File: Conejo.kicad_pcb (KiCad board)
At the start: 4 copper layers, 130.3 x 112.5 mm, 104 parts, among them J1 BATT, J2 HRO_TYPE-C-31-M-12, J3 JTAG_TC2030, J4 RGB, Q1 2N7002, Q2 2N7002, Q3 AO3407, SW1 POWER, SW10 MX Hotswap, SW11 MX Hotswap, SW12 MX Hotswap, SW13 MX Hotswap, SW14 MX Hotswap, SW15 MX Hotswap, SW16 MX Hotswap, SW17 MX Hotswap, SW18 MX Hotswap, SW19 MX Hotswap, SW2 MX Hotswap, SW20 MX Hotswap, SW21 MX Hotswap, SW22 MX Hotswap, SW23 MX Hotswap, SW24 MX Hotswap, SW25 MX Hotswap, SW26 MX Hotswap, SW27 MX Hotswap, SW28 MX Hotswap, SW29 RESET, SW3 MX Hotswap, SW4 MX Hotswap, SW5 MX Hotswap, SW6 MX Hotswap, SW7 MX Hotswap, SW8 MX Hotswap, SW9 MX Hotswap, U1 BQ24075RGT, U2 MAX17048, U3 SRV05-4, U4 MS88SF3

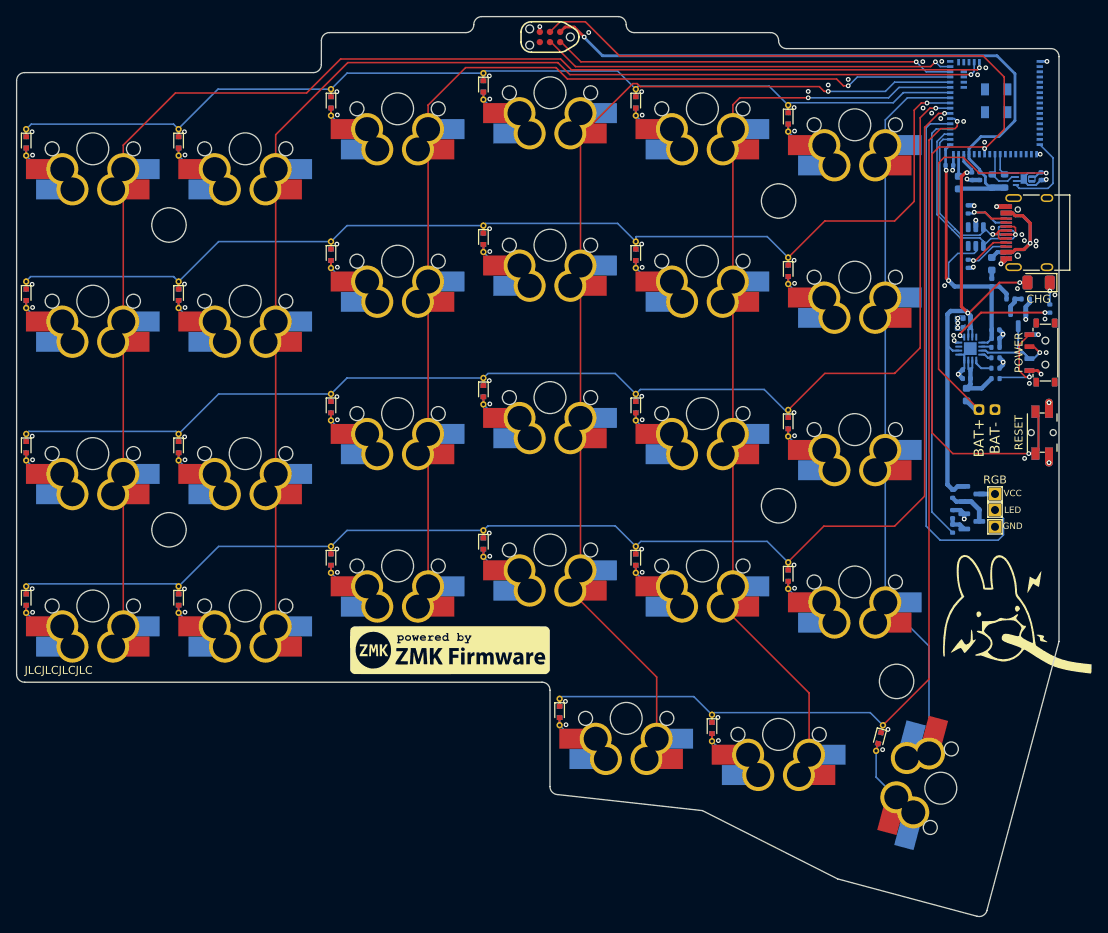
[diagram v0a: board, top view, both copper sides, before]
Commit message: feat(pcb): Version 0.4
- Prepare to move from JLC7628 stackup to JLC3313 stackup (Lowers dielectric constant from 4.6 to 4.05)
- Increase mounting hole diameter back to 5.4mm
- 6mil signals, 10mil power, 13 mil vias
  - 3W spacing wherever possible
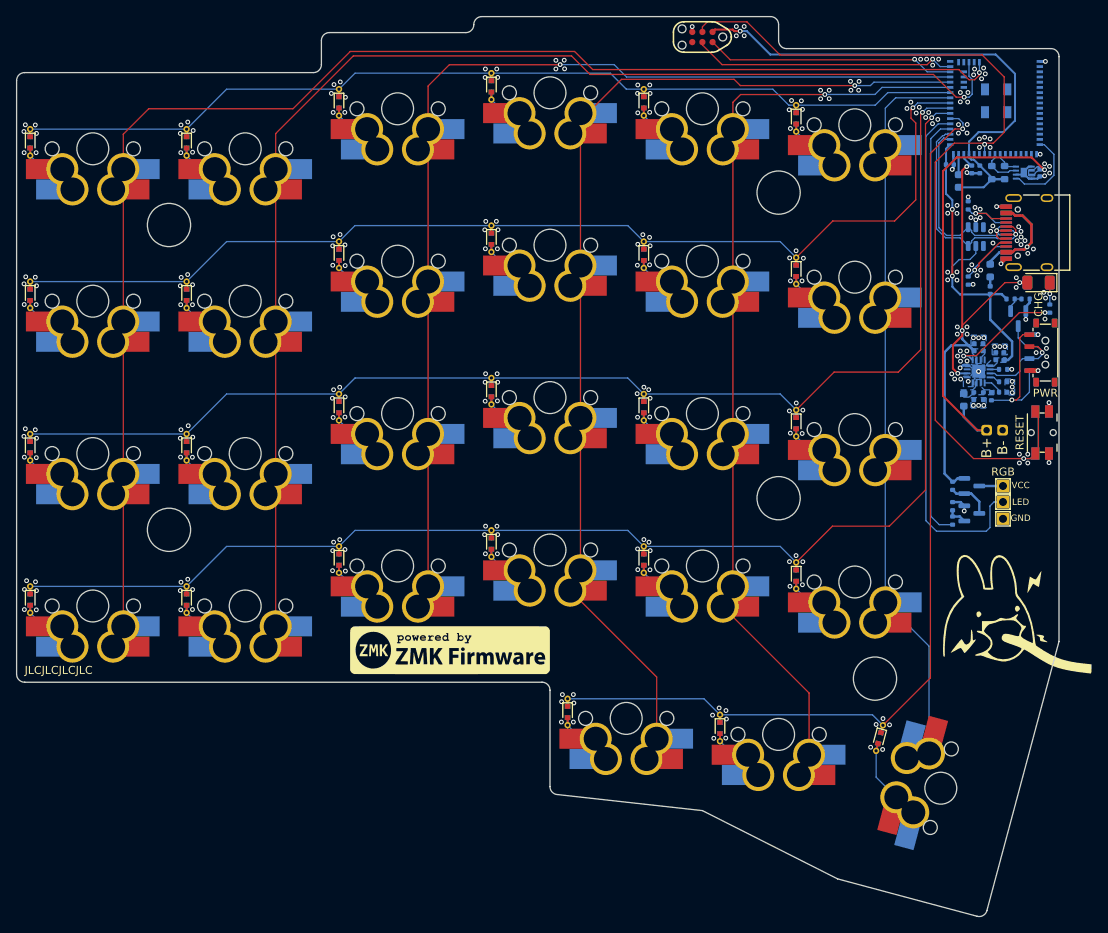
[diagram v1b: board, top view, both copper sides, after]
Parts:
- H1, H2, H3, H4, H5: footprint Conejo:MountingHole_4.3mm -> Conejo:MountingHole_5.4mm
- R4: value 100 -> 100R
- SW1: value POWER -> PWR
- moved J3 19.1 mm to (76.2, -12.0)
- moved C3 4.12 mm to (111.3, 26.8), turned to 90 degrees
- moved C7 3.42 mm to (110.1, 32.9), turned to -90 degrees
- moved C1 3.30 mm to (112.9, 27.9), turned to 90 degrees
- moved R2 3.15 mm to (113.8, 31.1)
- moved R3 3.15 mm to (113.8, 32.4)
- moved C6 3.04 mm to (111.3, 32.9), turned to -90 degrees
- moved U1 3.03 mm to (110.7, 29.8)
- moved R1 2.91 mm to (113.8, 29.6)
- moved J1 2.74 mm to (112.7, 37.2)
- moved H5 2.72 mm to (97.8, 68.2)
- moved C4 2.65 mm to (110.2, 26.8), turned to 90 degrees
- moved C2 2.43 mm to (113.9, 27.9), turned to -90 degrees
- moved R6 2.26 mm to (112.3, 32.9), turned to 90 degrees
- moved R9 2.10 mm to (109.4, 18.5)
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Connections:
- SW14 pad : (no net) -> COL4
- SW15 pad : (no net) -> COL4
- SW16 pad : (no net) -> COL4
- SW17 pad : (no net) -> COL4
- SW18 pad : (no net) -> COL4
- U3 pad 1: unconnected-(U3-Pad1) -> D-
- U3 pad 3: D- -> unconnected-(U3-Pad3)
- U3 pad 4: D+ -> unconnected-(U3-Pad4)
- U3 pad 6: unconnected-(U3-Pad6) -> D+
- U4 pad 54: unconnected-(U4-Pad54) -> COL2
- U4 pad 55: COL2 -> unconnected-(U4-Pad55)
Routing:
- net VDD: track 84.5 -> 64.9 mm
- net SWDIO: track 50.3 -> 31.3 mm
- net RESET: track 136.5 -> 117.6 mm
- net SWCLK: track 51.8 -> 33.2 mm
- net GND: track 40.2 -> 29.4 mm, vias 104 -> 290
- net VBAT: track 8.55 -> 0.00 mm
- net Net-(R6-Pad1): track 11.2 -> 17.8 mm
- net COL2: track 154.4 -> 159.1 mm
- net VDDH: track 64.5 -> 68.3 mm, vias 3 -> 4
- net +BATT: track 51.4 -> 54.9 mm
- net COL1: track 173.0 -> 176.1 mm
- net Net-(D16-Pad2): track 5.21 -> 2.39 mm
- net Net-(D17-Pad2): track 5.21 -> 2.39 mm
- net Net-(D8-Pad2): track 5.21 -> 2.39 mm
- net Net-(D23-Pad2): track 5.21 -> 2.39 mm
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- added copper zone on B.Cu, net +5V
- added copper zone on B.Cu, net VBAT
- added copper zone on B.Cu, net VDDH
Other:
- outline, holes or cut-outs redrawn
- board text added: "PWR"

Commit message: fix(pcb): Re-check GND vias around diodes
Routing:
- net GND: vias 290 -> 292
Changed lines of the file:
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@@
   (via (at 87.0712 34.766) (size 0.6) (drill 0.3302) (layers "F.Cu" "B.Cu") (net 2))
   (via (at 88.752824 53.618024) (size 0.6) (drill 0.3302) (layers "F.Cu" "B.Cu") (net 2))
+  (via (at 50.551255 -4.549705) (size 0.6) (drill 0.3302) (layers "F.Cu" "B.Cu") (net 2))
   (via (at 109.357448 -3.843509) (size 0.6) (drill 0.3302) (layers "F.Cu" "B.Cu") (net 2))
   (via (at -7.1882 -0.9791) (size 0.6) (drill 0.3302) (layers "F.Cu" "B.Cu") (net 2))
@@
   (via (at 10.9728 40.5318) (size 0.6) (drill 0.3302) (layers "F.Cu" "B.Cu") (net 2))
   (via (at 110.925 9.5469) (size 0.6) (drill 0.3302) (layers "F.Cu" "B.Cu") (net 2))
+  (via (at 49.09697 -4.552395) (size 0.6) (drill 0.3302) (layers "F.Cu" "B.Cu") (net 2))
   (via (at 116.873098 40.175) (size 0.6) (drill 0.3302) (layers "F.Cu" "B.Cu") (net 2))
   (via (at 106.864189 10.0518) (size 0.6) (drill 0.3302) (layers "F.Cu" "B.Cu") (net 2))

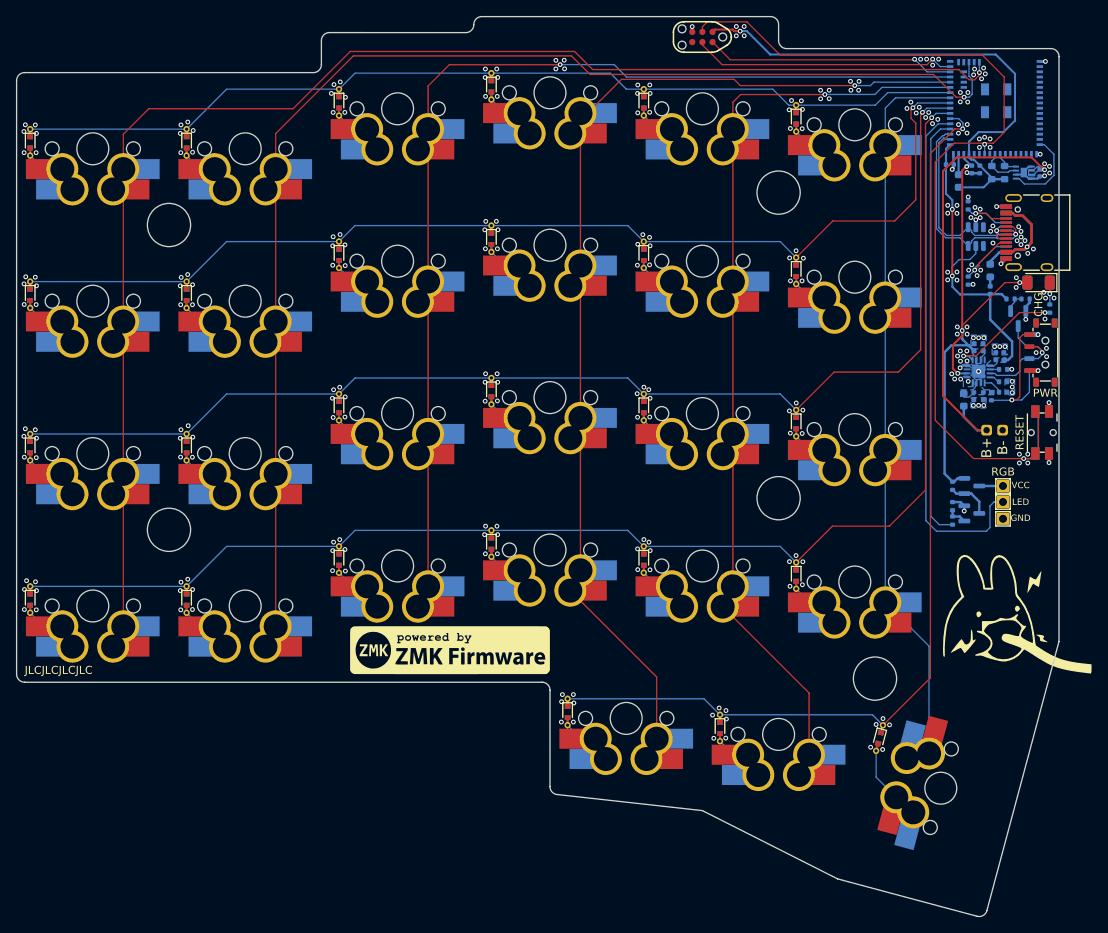
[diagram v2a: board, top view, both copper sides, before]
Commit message: feat(pcb): Version 0.4.1
- Add oscilloscope probing pads/labels
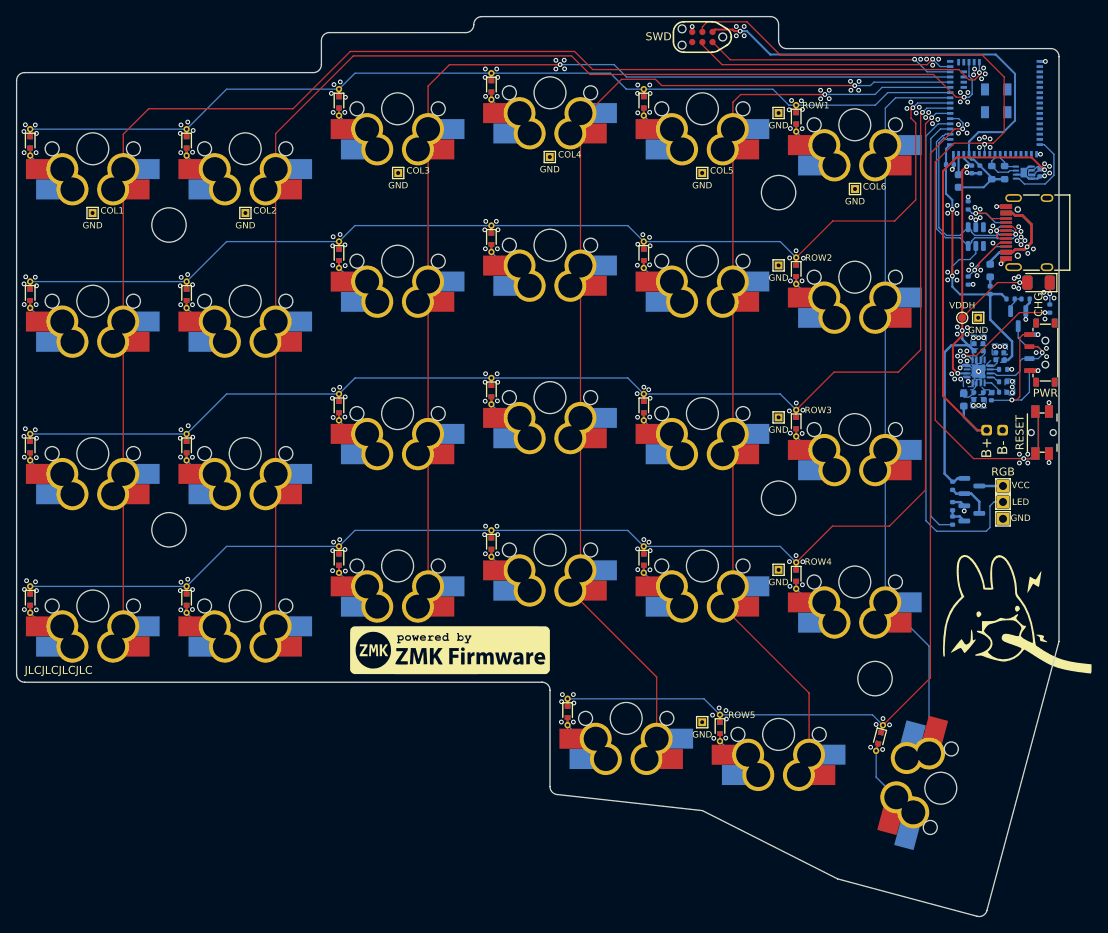
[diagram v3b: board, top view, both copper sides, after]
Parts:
- added TP1: GND, TestPoint:TestPoint_THTPad_1.0x1.0mm_Drill0.5mm, F.Cu at (95.3, 7.03)
- added TP1: GND, TestPoint:TestPoint_THTPad_1.0x1.0mm_Drill0.5mm, F.Cu at (85.7, 54.6)
- added TP1: GND, TestPoint:TestPoint_THTPad_1.0x1.0mm_Drill0.5mm, F.Cu at (-0.03, 10.0)
- added TP1: GND, TestPoint:TestPoint_THTPad_1.0x1.0mm_Drill0.5mm, F.Cu at (38.2, 5.03)
- added TP1: GND, TestPoint:TestPoint_THTPad_1.0x1.0mm_Drill0.5mm, F.Cu at (76.2, 5.03)
- added TP1: GND, TestPoint:TestPoint_THTPad_1.0x1.0mm_Drill0.5mm, F.Cu at (76.2, 73.7)
- added TP1: GND, TestPoint:TestPoint_THTPad_1.0x1.0mm_Drill0.5mm, F.Cu at (57.1, 3.02)
- added TP1: GND, TestPoint:TestPoint_THTPad_1.0x1.0mm_Drill0.5mm, F.Cu at (110.7, 23.1)
- added TP1: GND, TestPoint:TestPoint_THTPad_1.0x1.0mm_Drill0.5mm, F.Cu at (85.7, 16.6)
- added TP1: GND, TestPoint:TestPoint_THTPad_1.0x1.0mm_Drill0.5mm, F.Cu at (19.1, 10.0)
- added TP1: GND, TestPoint:TestPoint_THTPad_1.0x1.0mm_Drill0.5mm, F.Cu at (85.7, 35.6)
- added TP1: GND, TestPoint:TestPoint_THTPad_1.0x1.0mm_Drill0.5mm, F.Cu at (85.7, -2.48)
- added TP2: VDDH, TestPoint:TestPoint_Pad_D1.0mm, F.Cu at (108.7, 23.1)
- H1, H2, H3, H4, H5: footprint Conejo:MountingHole_5.4mm -> Conejo:MountingHole_4.3mm
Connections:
- SW14 pad : COL4 -> (no net)
- SW15 pad : COL4 -> (no net)
- SW16 pad : COL4 -> (no net)
- SW17 pad : COL4 -> (no net)
- SW18 pad : COL4 -> (no net)
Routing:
- net VDDH: track 68.3 -> 67.2 mm
- net GND: vias 292 -> 294
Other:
- board text added: "COL1"
- board text added: "COL2"
- board text added: "COL3"
- board text added: "COL4"
- board text added: "COL5"
- board text added: "COL6"
- board text added: "ROW1"
- board text added: "ROW2"
- board text added: "ROW3"
- board text added: "ROW4"
- board text added: "ROW5"
- board text added: "SWD"
